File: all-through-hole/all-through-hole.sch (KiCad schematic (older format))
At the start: 21 parts, among them J1 Conn_01x01, J2 Conn_01x01, SW1 SW_SPST, U1 MC34063AP, U2 LF90_TO220

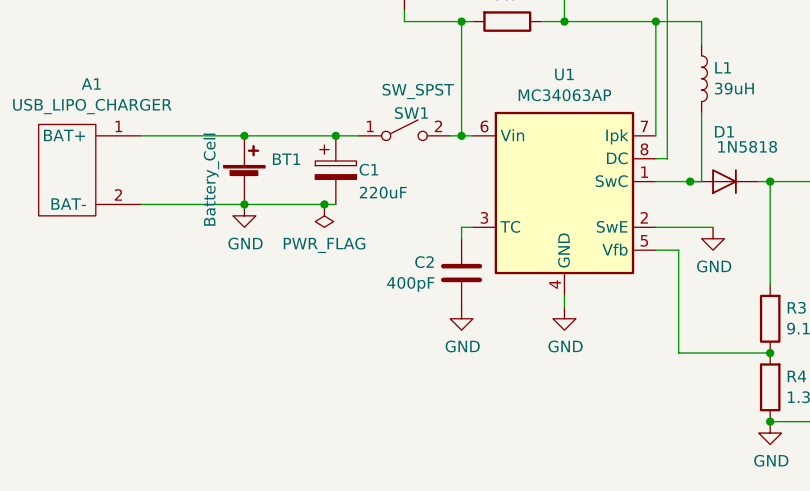
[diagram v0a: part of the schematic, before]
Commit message: Associate footprints for all-through-hole
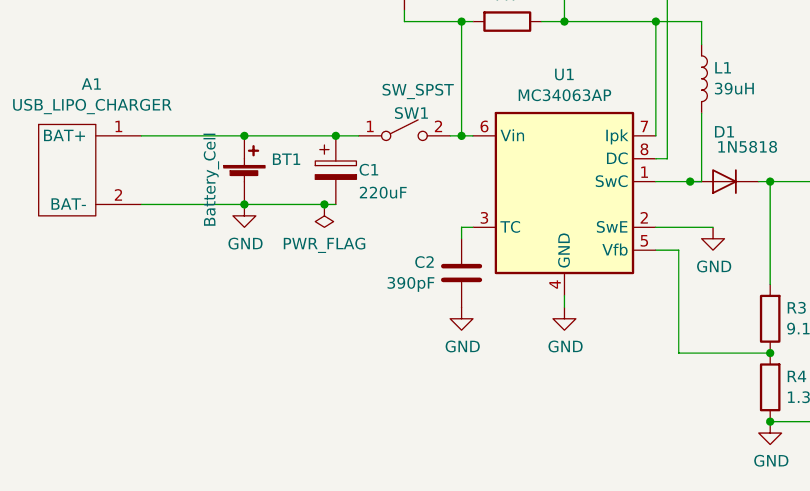
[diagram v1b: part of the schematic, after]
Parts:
- A1: footprint (none) -> homebrew:USB_LIPO_CHARGER_TP4056
- BT1: footprint (none) -> homebrew:1043P_18650_holder
- C1, C3: footprint (none) -> Capacitor_THT:CP_Radial_D6.3mm_P2.50mm
- C2: value 400pF -> 390pF; footprint (none) -> Capacitor_THT:C_Disc_D5.0mm_W2.5mm_P5.00mm
- C4: footprint (none) -> Capacitor_SMD:C_0603_1608Metric_Pad1.05x0.95mm_HandSolder
- C5: footprint (none) -> Capacitor_THT:C_Disc_D5.1mm_W3.2mm_P5.00mm
- C6: footprint (none) -> Capacitor_THT:CP_Radial_D5.0mm_P2.00mm
- D1: footprint (none) -> Diode_THT:D_DO-41_SOD81_P7.62mm_Horizontal
- D2: footprint (none) -> LED_THT:LED_D5.0mm_Horizontal_O3.81mm_Z9.0mm
- J1, J2: footprint (none) -> Connector_PinHeader_2.54mm:PinHeader_1x01_P2.54mm_Vertical
- L1: footprint (none) -> Inductor_THT:L_Toroid_Vertical_L21.6mm_W9.1mm_P8.40mm_Bourns_5700
- R1, R2, R3, R4, R5: footprint (none) -> Resistor_THT:R_Axial_DIN0207_L6.3mm_D2.5mm_P10.16mm_Horizontal
- SW1: footprint (none) -> homebrew:‎EG1206‎_SLIDE_SWITCH
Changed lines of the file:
@@
 F 0 "C5" H 5915 5146 50  0000 L CNN
 F 1 "0.1uF" H 5915 5055 50  0000 L CNN
-F 2 "" H 5838 4950 50  0001 C CNN
+F 2 "Capacitor_THT:C_Disc_D5.1mm_W3.2mm_P5.00mm" H 5838 4950 50  0001 C CNN
 F 3 "~" H 5800 5100 50  0001 C CNN
 	1    5800 5100
@@
 F 0 "C4" H 5215 5146 50  0000 L CNN
 F 1 "0.1uF_SMD" H 5215 5055 50  0000 L CNN
-F 2 "" H 5138 4950 50  0001 C CNN
+F 2 "Capacitor_SMD:C_0603_1608Metric_Pad1.05x0.95mm_HandSolder" H 5138 4950 50  0001 C CNN
 F 3 "~" H 5100 5100 50  0001 C CNN
 	1    5100 5100
@@
 F 0 "C6" H 6818 5146 50  0000 L CNN
 F 1 "2.2uF" H 6818 5055 50  0000 L CNN
-F 2 "" H 6738 4950 50  0001 C CNN
+F 2 "Capacitor_THT:CP_Radial_D5.0mm_P2.00mm" H 6738 4950 50  0001 C CNN
 F 3 "~" H 6700 5100 50  0001 C CNN
 	1    6700 5100
@@
 F 0 "BT1" H 1668 5146 50  0000 L CNN
 F 1 "Battery_Cell" V 1400 4850 50  0000 L CNN
-F 2 "" V 1550 5110 50  0001 C CNN
+F 2 "homebrew:1043P_18650_holder" V 1550 5110 50  0001 C CNN
 F 3 "~" V 1550 5110 50  0001 C CNN
 	1    1550 5050
@@
 F 0 "C1" H 2050 5000 50  0000 L CNN
 F 1 "220uF" H 2050 4900 50  0000 L CNN
-F 2 "" H 1988 4850 50  0001 C CNN
+F 2 "Capacitor_THT:CP_Radial_D6.3mm_P2.50mm" H 1988 4850 50  0001 C CNN
 F 3 "~" H 1950 5000 50  0001 C CNN
 	1    1950 5000
@@
 F 0 "D1" H 3650 4834 50  0000 C CNN
 F 1 "1N5818" H 3550 4900 50  0000 C CNN
-F 2 "" H 3650 5050 50  0001 C CNN
+F 2 "Diode_THT:D_DO-41_SOD81_P7.62mm_Horizontal" H 3650 5050 50  0001 C CNN
 F 3 "~" H 3650 5050 50  0001 C CNN
 	1    3650 5050
@@
 F 0 "C3" H 4268 5296 50  0000 L CNN
 F 1 "220uF" H 4268 5205 50  0000 L CNN
-F 2 "" H 4188 5100 50  0001 C CNN
+F 2 "Capacitor_THT:CP_Radial_D6.3mm_P2.50mm" H 4188 5100 50  0001 C CNN
 F 3 "~" H 4150 5250 50  0001 C CNN
 	1    4150 5250
@@
 F 0 "SW1" H 2204 4948 50  0000 L CNN
 F 1 "SW_SPST" H 2150 5050 50  0000 L CNN
-F 2 "" H 2250 4850 50  0001 C CNN
+F 2 "homebrew:‎EG1206‎_SLIDE_SWITCH" H 2250 4850 50  0001 C CNN
 F 3 "~" H 2250 4850 50  0001 C CNN
 	1    2250 4850
@@
 P 2500 5450
 F 0 "C2" H 2615 5496 50  0000 L CNN
-F 1 "400pF" H 2615 5405 50  0000 L CNN
-F 2 "" H 2538 5300 50  0001 C CNN
+F 1 "390pF" H 2615 5405 50  0000 L CNN
+F 2 "Capacitor_THT:C_Disc_D5.0mm_W2.5mm_P5.00mm" H 2538 5300 50  0001 C CNN
 F 3 "~" H 2500 5450 50  0001 C CNN
 	1    2500 5450
@@
 F 0 "R1" V 2493 4350 50  0000 C CNN
 F 1 ".47" V 2584 4350 50  0000 C CNN
-F 2 "" V 2630 4350 50  0001 C CNN
+F 2 "Resistor_THT:R_Axial_DIN0207_L6.3mm_D2.5mm_P10.16mm_Horizontal" V 2630 4350 50  0001 C CNN
 F 3 "~" H 2700 4350 50  0001 C CNN
 	1    2700 4350
@@
 F 0 "R2" V 2893 4200 50  0000 C CNN
 F 1 "180" V 2984 4200 50  0000 C CNN
-F 2 "" V 3030 4200 50  0001 C CNN
+F 2 "Resistor_THT:R_Axial_DIN0207_L6.3mm_D2.5mm_P10.16mm_Horizontal" V 3030 4200 50  0001 C CNN
 F 3 "~" H 3100 4200 50  0001 C CNN
 	1    3100 4200
@@
 F 0 "L1" H 3603 4646 50  0000 L CNN
 F 1 "39uH" H 3603 4555 50  0000 L CNN
-F 2 "" H 3550 4600 50  0001 C CNN
+F 2 "Inductor_THT:L_Toroid_Vertical_L21.6mm_W9.1mm_P8.40mm_Bourns_5700" H 3550 4600 50  0001 C CNN
 F 3 "~" H 3550 4600 50  0001 C CNN
 	1    3550 4600
@@
 F 0 "R3" H 3780 5604 50  0000 R CNN
 F 1 "9.1k" H 3780 5695 50  0000 R CNN
-F 2 "" V 3780 5650 50  0001 C CNN
+F 2 "Resistor_THT:R_Axial_DIN0207_L6.3mm_D2.5mm_P10.16mm_Horizontal" V 3780 5650 50  0001 C CNN
 F 3 "~" H 3850 5650 50  0001 C CNN
 	1    3850 5650
@@
 F 0 "R4" H 3780 5904 50  0000 R CNN
 F 1 "1.3k" H 3780 5995 50  0000 R CNN
-F 2 "" V 3780 5950 50  0001 C CNN
+F 2 "Resistor_THT:R_Axial_DIN0207_L6.3mm_D2.5mm_P10.16mm_Horizontal" V 3780 5950 50  0001 C CNN
 F 3 "~" H 3850 5950 50  0001 C CNN
 	1    3850 5950
@@
 F 0 "J1" V 4568 5180 50  0000 L CNN
 F 1 "Conn_01x01" V 4613 5180 50  0001 L CNN
-F 2 "" H 4650 5100 50  0001 C CNN
+F 2 "Connector_PinHeader_2.54mm:PinHeader_1x01_P2.54mm_Vertical" H 4650 5100 50  0001 C CNN
 F 3 "~" H 4650 5100 50  0001 C CNN
 	1    4650 5100
@@
 F 0 "J2" V 7118 5180 50  0000 L CNN
 F 1 "Conn_01x01" V 7163 5180 50  0001 L CNN
-F 2 "" H 7200 5100 50  0001 C CNN
+F 2 "Connector_PinHeader_2.54mm:PinHeader_1x01_P2.54mm_Vertical" H 7200 5100 50  0001 C CNN
 F 3 "~" H 7200 5100 50  0001 C CNN
 	1    7200 5100
@@
 F 0 "D2" V 7689 4933 50  0000 R CNN
 F 1 "LED" V 7598 4933 50  0000 R CNN
-F 2 "" H 7650 5050 50  0001 C CNN
+F 2 "LED_THT:LED_D5.0mm_Horizontal_O3.81mm_Z9.0mm" H 7650 5050 50  0001 C CNN
 F 3 "~" H 7650 5050 50  0001 C CNN
 	1    7650 5050
@@
 F 0 "R5" H 7720 5396 50  0000 L CNN
 F 1 "10k" H 7720 5305 50  0000 L CNN
-F 2 "" V 7580 5350 50  0001 C CNN
+F 2 "Resistor_THT:R_Axial_DIN0207_L6.3mm_D2.5mm_P10.16mm_Horizontal" V 7580 5350 50  0001 C CNN
 F 3 "~" H 7650 5350 50  0001 C CNN
 	1    7650 5350
@@
 F 0 "A1" H 883 5375 50  0000 C CNN
 F 1 "USB_LIPO_CHARGER" H 883 5284 50  0000 C CNN
-F 2 "" H 850 5000 50  0001 C CNN
+F 2 "homebrew:USB_LIPO_CHARGER_TP4056" H 850 5000 50  0001 C CNN
 F 3 "" H 850 5000 50  0001 C CNN
 	1    850  5000

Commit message: First pass at layout
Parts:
- added H? (x4): HOLE, symbol Homebrew:HOLE
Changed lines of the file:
@@
 Wire Wire Line
 	3350 5250 3600 5250
+$Comp
+L Homebrew:HOLE H?
+U 1 1 5E7F33D9
+P 4500 3050
+F 0 "H?" H 4609 3103 60  0000 L CNN
+F 1 "HOLE" H 4609 2997 60  0000 L CNN
+F 2 "" H 4500 3050 60  0001 C CNN
+F 3 "" H 4500 3050 60  0001 C CNN
+	1    4500 3050
+	1    0    0    -1
+$EndComp
+$Comp
+L Homebrew:HOLE H?
+U 1 1 5E7F3D5C
+P 4500 3300
+F 0 "H?" H 4609 3353 60  0000 L CNN
+F 1 "HOLE" H 4609 3247 60  0000 L CNN
+F 2 "" H 4500 3300 60  0001 C CNN
+F 3 "" H 4500 3300 60  0001 C CNN
+	1    4500 3300
+	1    0    0    -1
+$EndComp
+$Comp
+L Homebrew:HOLE H?
+U 1 1 5E7F3FDF
+P 4500 3550
+F 0 "H?" H 4609 3603 60  0000 L CNN
+F 1 "HOLE" H 4609 3497 60  0000 L CNN
+F 2 "" H 4500 3550 60  0001 C CNN
+F 3 "" H 4500 3550 60  0001 C CNN
+	1    4500 3550
+	1    0    0    -1
+$EndComp
+$Comp
+L Homebrew:HOLE H?
+U 1 1 5E7F4298
+P 4500 3800
+F 0 "H?" H 4609 3853 60  0000 L CNN
+F 1 "HOLE" H 4609 3747 60  0000 L CNN
+F 2 "" H 4500 3800 60  0001 C CNN
+F 3 "" H 4500 3800 60  0001 C CNN
+	1    4500 3800
+	1    0    0    -1
+$EndComp
 $EndSCHEMATC

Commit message: Hardware v1.0
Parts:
- H1, H2, H3, H4: renamed from H?; footprint (none) -> homebrew:HOLE_5MM_#8
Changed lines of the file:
@@
 	3350 5250 3600 5250
 $Comp
-L Homebrew:HOLE H?
+L Homebrew:HOLE H1
 U 1 1 5E7F33D9
 P 4500 3050
-F 0 "H?" H 4609 3103 60  0000 L CNN
+F 0 "H1" H 4609 3103 60  0000 L CNN
 F 1 "HOLE" H 4609 2997 60  0000 L CNN
-F 2 "" H 4500 3050 60  0001 C CNN
+F 2 "homebrew:HOLE_5MM_#8" H 4500 3050 60  0001 C CNN
 F 3 "" H 4500 3050 60  0001 C CNN
 	1    4500 3050
@@
 $EndComp
 $Comp
-L Homebrew:HOLE H?
+L Homebrew:HOLE H2
 U 1 1 5E7F3D5C
 P 4500 3300
-F 0 "H?" H 4609 3353 60  0000 L CNN
+F 0 "H2" H 4609 3353 60  0000 L CNN
 F 1 "HOLE" H 4609 3247 60  0000 L CNN
-F 2 "" H 4500 3300 60  0001 C CNN
+F 2 "homebrew:HOLE_5MM_#8" H 4500 3300 60  0001 C CNN
 F 3 "" H 4500 3300 60  0001 C CNN
 	1    4500 3300
@@
 $EndComp
 $Comp
-L Homebrew:HOLE H?
+L Homebrew:HOLE H3
 U 1 1 5E7F3FDF
 P 4500 3550
-F 0 "H?" H 4609 3603 60  0000 L CNN
+F 0 "H3" H 4609 3603 60  0000 L CNN
 F 1 "HOLE" H 4609 3497 60  0000 L CNN
-F 2 "" H 4500 3550 60  0001 C CNN
+F 2 "homebrew:HOLE_5MM_#8" H 4500 3550 60  0001 C CNN
 F 3 "" H 4500 3550 60  0001 C CNN
 	1    4500 3550
@@
 $EndComp
 $Comp
-L Homebrew:HOLE H?
+L Homebrew:HOLE H4
 U 1 1 5E7F4298
 P 4500 3800
-F 0 "H?" H 4609 3853 60  0000 L CNN
+F 0 "H4" H 4609 3853 60  0000 L CNN
 F 1 "HOLE" H 4609 3747 60  0000 L CNN
-F 2 "" H 4500 3800 60  0001 C CNN
+F 2 "homebrew:HOLE_5MM_#8" H 4500 3800 60  0001 C CNN
 F 3 "" H 4500 3800 60  0001 C CNN
 	1    4500 3800
